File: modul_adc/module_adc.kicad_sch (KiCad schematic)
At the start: 26 parts

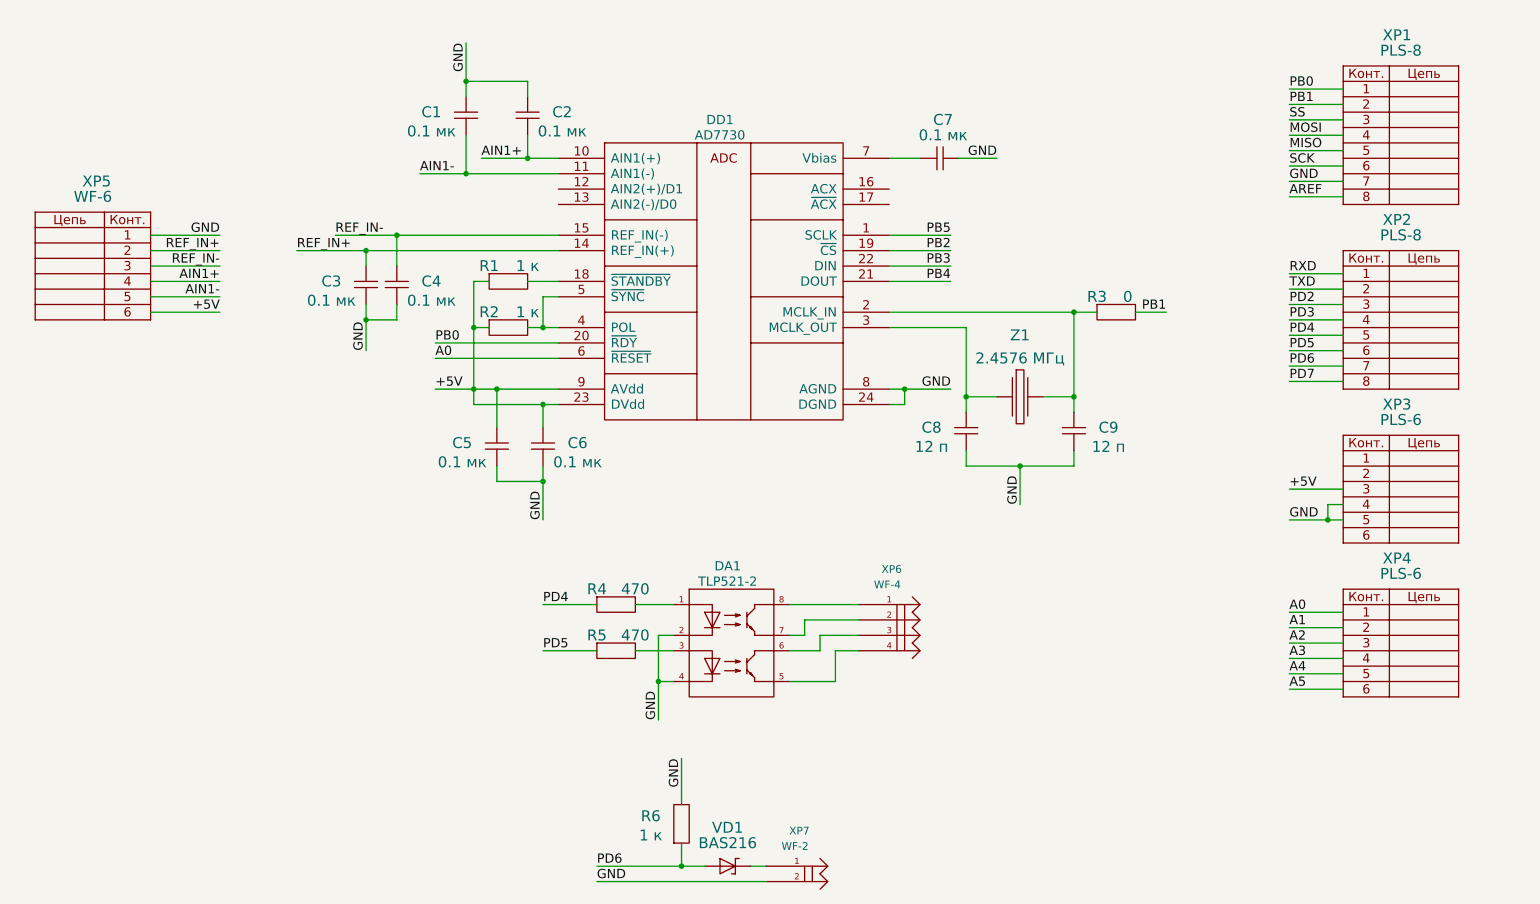
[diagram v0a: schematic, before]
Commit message: Дополнил схему ацп для тензодатчика и приступил к трассировке печатной платы.
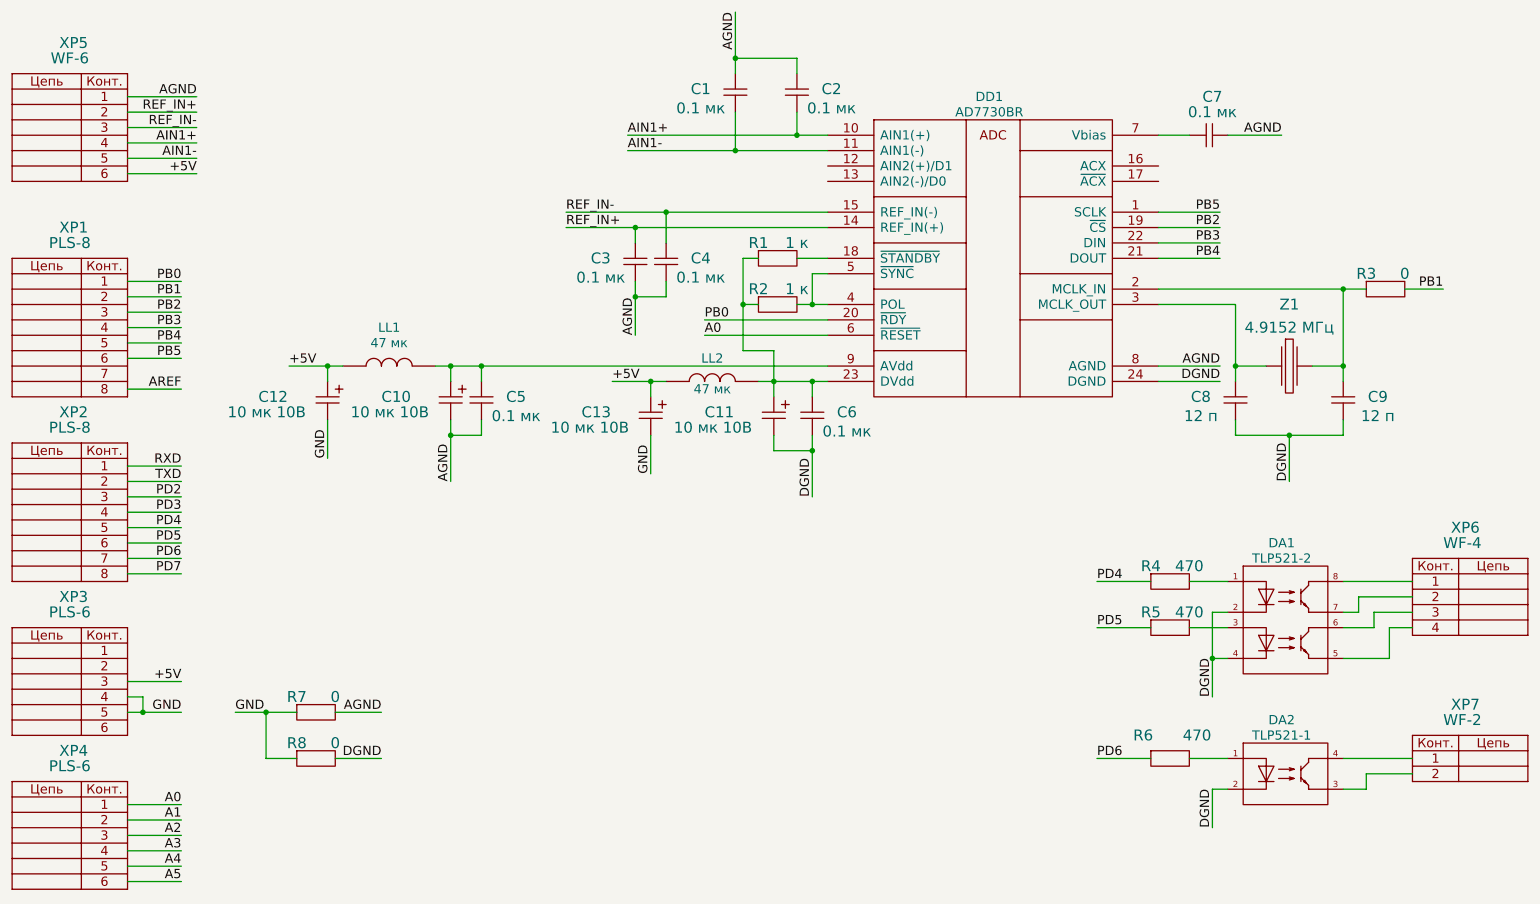
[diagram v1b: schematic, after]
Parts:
- removed VD1: BAS216, IWcomponents:SOD110, symbol module_adc-rescue:SHOTTKY_DIODE
- removed XP6: WF-4, IWconnectors:WF-4, symbol module_adc-rescue:PIN_M_4
- removed XP7: WF-2, IWconnectors:WF-2, symbol module_adc-rescue:PIN_M_2
- added C10, C11, C12, C13: 10 мк 10В, IWsmd_case:CASE_B, symbol LFcapitors:CAPITORS_ELECTROLYTIC
- added DA2: TLP521-1, IWcomponents:DIP_4, symbol LFcomponents:TLP521-1
- added LL1, LL2: 47 мк, IWsmd_case:SMD0805, symbol LFtransformator:INDUCTOR_3
- added R7, R8: 0, IWsmd_case:SMD0805, symbol module_adc-rescue:RESISTOR
- added XP6: WF-4, IWconnectors:WF-4, symbol LFconnectors:connector_4pin_gost
- added XP7: WF-2, IWconnectors:WF-2, symbol LFconnectors:connector_2pin_gost
- DD1: value AD7730 -> AD7730BR
- R6: value 1 к -> 470
- Z1: value 2.4576 МГц -> 4.9152 МГц; footprint IWcomponents:Q_49U3HMS& -> IWcomponents:HC-49SM
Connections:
- net MISO is gone; now on net PB4: XP1.5
- net MOSI is gone; now on net PB3: XP1.4
- net SCK is gone; now on net PB5: XP1.6
- net SS is gone; now on net PB2: XP1.3
- net +5V: now also C12.1, C13.1, LL1.2, LL2.2; no longer C5.1, C6.1, DD1.23 (DVdd), DD1.9 (AVdd), R1.1, R2.1
- net GND: now also C12.2, C13.2, R7.1, R8.1; no longer C1.1, C2.1, C3.2, C4.2, C5.2, C6.2, C7.1, C8.2, C9.2, DA1.2, DA1.4, DD1.24 (DGND), DD1.8 (AGND), R6.2, XP1.7, XP5.1
- net at DA1.5: now also XP6.4
- net at DA1.6: now also XP6.3
- net at DA1.7: now also XP6.2
- net at DA1.8: now also XP6.1
- new net: C11.1, C6.1, DD1.23 (DVdd), LL2.1, R1.1, R2.1
- new net: C10.1, C5.1, DD1.9 (AVdd), LL1.1
- new net: DA2.1, R6.2
- new net: DA2.4, XP7.1
- new net: DA2.3, XP7.2
- new net AGND: C1.1, C10.2, C2.1, C3.2, C4.2, C5.2, C7.1, DD1.8 (AGND), R7.2, XP5.1
- new net DGND: C11.2, C6.2, C8.2, C9.2, DA1.2, DA1.4, DA2.2, DD1.24 (DGND), R8.2
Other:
- moved on the sheet: C1, C2, C3, C4, C5, C6, C7, C8, C9, DA1, DD1, R1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

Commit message: Добавил обозначение разъёмов на схеме, поправил посадочное место кварца и отправил плату в производство.
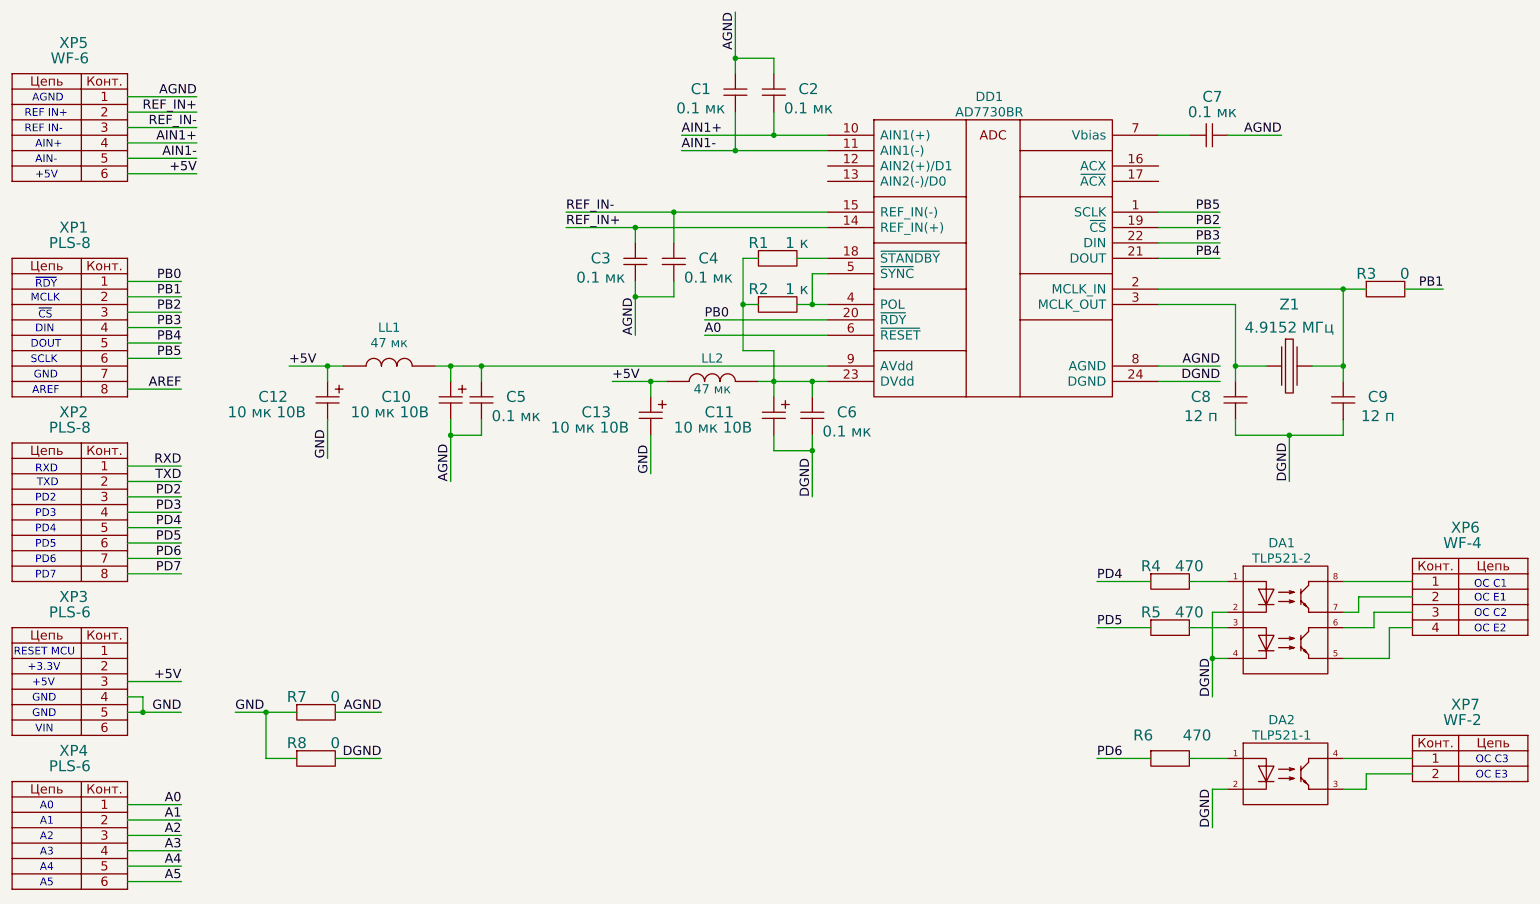
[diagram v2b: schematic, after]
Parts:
- Z1: footprint IWcomponents:HC-49SM -> IWcrystal_oscil:HC-49U
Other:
- note added: "+3.3V"
- note added: "+5V"
- note added: "A0"
- note added: "A1"
- note added: "A2"
- note added: "A3"
- note added: "A4"
- note added: "A5"
- note added: "AGND"
- note added: "AIN+"
- note added: "AIN-"
- note added: "AREF"
- note added: "DIN"
- note added: "DOUT"
- note added: "GND"
- note added: "MCLK"
- note added: "OC C1"
- note added: "OC C2"
- note added: "OC C3"
- note added: "OC E1"
- note added: "OC E2"
- note added: "OC E3"
- note added: "PD2"
- note added: "PD3"
- note added: "PD4"
- note added: "PD5"
- note added: "PD6"
- note added: "PD7"
- note added: "REF IN+"
- note added: "REF IN-"
- note added: "RESET MCU"
- note added: "RXD"
- note added: "SCLK"
- note added: "TXD"
- note added: "VIN"
- note added: "~{CS}"
- note added: "~{RDY}"
- moved on the sheet: C2, C4
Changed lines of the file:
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@@
   (junction (at 140.97 72.39) (diameter 0) (color 0 0 0 0)
   )
-  (junction (at 128.27 57.15) (diameter 0) (color 0 0 0 0)
+  (junction (at 129.54 57.15) (diameter 0) (color 0 0 0 0)
   )
   (junction (at 231.14 93.98) (diameter 0) (color 0 0 0 0)
   )
-  (junction (at 149.86 44.45) (diameter 0) (color 0 0 0 0)
+  (junction (at 146.05 44.45) (diameter 0) (color 0 0 0 0)
   )
   (junction (at 92.71 82.55) (diameter 0) (color 0 0 0 0)
@@
     (stroke (width 0) (type default))
   )
-  (wire (pts (xy 121.92 44.45) (xy 149.86 44.45))
+  (wire (pts (xy 130.81 44.45) (xy 146.05 44.45))
     (stroke (width 0) (type default))
   )
@@
     (stroke (width 0) (type default))
   )
-  (wire (pts (xy 128.27 57.15) (xy 154.94 57.15))
+  (wire (pts (xy 129.54 57.15) (xy 154.94 57.15))
     (stroke (width 0) (type default))
   )
@@
     (stroke (width 0) (type default))
   )
-  (wire (pts (xy 121.92 46.99) (xy 139.7 46.99))
+  (wire (pts (xy 130.81 46.99) (xy 139.7 46.99))
     (stroke (width 0) (type default))
   )
@@
     (stroke (width 0) (type default))
   )
-  (wire (pts (xy 149.86 40.64) (xy 149.86 44.45))
+  (wire (pts (xy 146.05 40.64) (xy 146.05 44.45))
     (stroke (width 0) (type default))
   )
@@
     (stroke (width 0) (type default))
   )
-  (wire (pts (xy 128.27 68.58) (xy 128.27 71.12))
+  (wire (pts (xy 129.54 68.58) (xy 129.54 71.12))
     (stroke (width 0) (type default))
   )
@@
     (stroke (width 0) (type default))
   )
-  (wire (pts (xy 128.27 71.12) (xy 123.19 71.12))
+  (wire (pts (xy 129.54 71.12) (xy 123.19 71.12))
     (stroke (width 0) (type default))
   )
@@
     (stroke (width 0) (type default))
   )
-  (wire (pts (xy 111.76 57.15) (xy 128.27 57.15))
+  (wire (pts (xy 111.76 57.15) (xy 129.54 57.15))
     (stroke (width 0) (type default))
   )
@@
     (stroke (width 0) (type default))
   )
-  (wire (pts (xy 128.27 62.23) (xy 128.27 57.15))
+  (wire (pts (xy 129.54 62.23) (xy 129.54 57.15))
     (stroke (width 0) (type default))
   )
@@
     (stroke (width 0) (type default))
   )
-  (wire (pts (xy 139.7 31.75) (xy 149.86 31.75))
+  (wire (pts (xy 139.7 31.75) (xy 146.05 31.75))
     (stroke (width 0) (type default))
   )
@@
     (stroke (width 0) (type default))
   )
-  (wire (pts (xy 149.86 31.75) (xy 149.86 34.29))
+  (wire (pts (xy 146.05 31.75) (xy 146.05 34.29))
     (stroke (width 0) (type default))
   )
@@
     (stroke (width 0) (type default))
   )
-  (wire (pts (xy 149.86 44.45) (xy 154.94 44.45))
+  (wire (pts (xy 146.05 44.45) (xy 154.94 44.45))
     (stroke (width 0) (type default))
   )
@@
     (stroke (width 0) (type default))
   )
+  (text "RESET MCU" (at 20.574 130.556 0)
+    (effects (font (size 1.27 1.27)) (justify left bottom))
+  )
+  (text "A2" (at 24.892 161.036 0)
+    (effects (font (size 1.27 1.27)) (justify left bottom))
+  )
+  (text "PD7" (at 24.13 117.856 0)
+    (effects (font (size 1.27 1.27)) (justify left bottom))
+  )
+  (text "PD4" (at 24.13 110.236 0)
+    (effects (font (size 1.27 1.27)) (justify left bottom))
+  )
+  (text "+5V" (at 24.13 51.816 0)
+    (effects (font (size 1.27 1.27)) (justify left bottom))
+  )
+  (text "OC E2" (at 261.62 126.746 0)
+    (effects (font (size 1.27 1.27)) (justify left bottom))
+  )
+  (text "MCLK" (at 23.368 72.136 0)
+    (effects (font (size 1.27 1.27)) (justify left bottom))
+  )
+  (text "OC C3" (at 261.874 148.336 0)
+    (effects (font (size 1.27 1.27)) (justify left bottom))
+  )
+  (text "RXD" (at 24.13 100.33 0)
+    (effects (font (size 1.27 1.27)) (justify left bottom))
+  )
+  (text "A5" (at 24.892 168.656 0)
+    (effects (font (size 1.27 1.27)) (justify left bottom))
+  )
+  (text "REF IN-" (at 22.352 44.196 0)
+    (effects (font (size 1.27 1.27)) (justify left bottom))
+  )
+  (text "TXD" (at 24.384 102.616 0)
+    (effects (font (size 1.27 1.27)) (justify left bottom))
+  )
+  (text "PD6" (at 24.13 115.316 0)
+    (effects (font (size 1.27 1.27)) (justify left bottom))
+  )
+  (text "PD2" (at 24.13 105.156 0)
+    (effects (font (size 1.27 1.27)) (justify left bottom))
+  )
+  (text "OC E1" (at 261.62 121.666 0)
+    (effects (font (size 1.27 1.27)) (justify left bottom))
+  )
+  (text "AGND" (at 23.622 39.116 0)
+    (effects (font (size 1.27 1.27)) (justify left bottom))
+  )
+  (text "VIN" (at 24.13 143.256 0)
+    (effects (font (size 1.27 1.27)) (justify left bottom))
+  )
+  (text "GND" (at 23.622 138.176 0)
+    (effects (font (size 1.27 1.27)) (justify left bottom))
+  )
+  (text "A3" (at 24.892 163.576 0)
+    (effects (font (size 1.27 1.27)) (justify left bottom))
+  )
+  (text "+5V" (at 23.622 135.636 0)
+    (effects (font (size 1.27 1.27)) (justify left bottom))
+  )
+  (text "OC C1" (at 261.62 119.38 0)
+    (effects (font (size 1.27 1.27)) (justify left bottom))
+  )
+  (text "AREF" (at 23.622 87.376 0)
+    (effects (font (size 1.27 1.27)) (justify left bottom))
+  )
+  (text "A1" (at 24.892 158.496 0)
+    (effects (font (size 1.27 1.27)) (justify left bottom))
+  )
+  (text "~{CS}" (at 24.638 74.93 0)
+    (effects (font (size 1.27 1.27)) (justify left bottom))
+  )
+  (text "OC E3" (at 261.874 150.876 0)
+    (effects (font (size 1.27 1.27)) (justify left bottom))
+  )
+  (text "A0" (at 24.892 155.956 0)
+    (effects (font (size 1.27 1.27)) (justify left bottom))
+  )
+  (text "GND" (at 23.622 140.716 0)
+    (effects (font (size 1.27 1.27)) (justify left bottom))
+  )
+  (text "GND" (at 23.876 84.836 0)
+    (effects (font (size 1.27 1.27)) (justify left bottom))
+  )
+  (text "AIN-" (at 24.13 49.276 0)
+    (effects (font (size 1.27 1.27)) (justify left bottom))
+  )
+  (text "OC C2" (at 261.62 124.206 0)
+    (effects (font (size 1.27 1.27)) (justify left bottom))
+  )
+  (text "A4" (at 24.892 166.116 0)
+    (effects (font (size 1.27 1.27)) (justify left bottom))
+  )
+  (text "DOUT" (at 23.368 79.756 0)
+    (effects (font (size 1.27 1.27)) (justify left bottom))
+  )
+  (text "AIN+" (at 24.13 46.736 0)
+    (effects (font (size 1.27 1.27)) (justify left bottom))
+  )
+  (text "DIN" (at 24.13 77.216 0)
+    (effects (font (size 1.27 1.27)) (justify left bottom))
+  )
+  (text "PD3" (at 24.13 107.696 0)
+    (effects (font (size 1.27 1.27)) (justify left bottom))
+  )
+  (text "~{RDY}" (at 24.13 69.85 0)
+    (effects (font (size 1.27 1.27)) (justify left bottom))
+  )
+  (text "PD5" (at 24.13 112.776 0)
+    (effects (font (size 1.27 1.27)) (justify left bottom))
+  )
+  (text "+3.3V" (at 22.86 133.096 0)
+    (effects (font (size 1.27 1.27)) (justify left bottom))
+  )
+  (text "REF IN+" (at 22.352 41.656 0)
+    (effects (font (size 1.27 1.27)) (justify left bottom))
+  )
+  (text "SCLK" (at 23.368 82.296 0)
+    (effects (font (size 1.27 1.27)) (justify left bottom))
+  )
   (label "REF_IN-" (at 111.76 57.15 0) (fields_autoplaced)
     (effects (font (size 1.524 1.524)) (justify left bottom))
@@
     (effects (font (size 1.524 1.524)) (justify right bottom))
   )
-  (label "AIN1-" (at 121.92 46.99 0) (fields_autoplaced)
+  (label "AIN1-" (at 130.81 46.99 0) (fields_autoplaced)
     (effects (font (size 1.524 1.524)) (justify left bottom))
   )
@@
     (effects (font (size 1.524 1.524)) (justify left bottom))
   )
-  (label "AIN1+" (at 121.92 44.45 0) (fields_autoplaced)
+  (label "AIN1+" (at 130.81 44.45 0) (fields_autoplaced)
     (effects (font (size 1.524 1.524)) (justify left bottom))
   )
@@
     )
   )
-  (symbol (lib_id "module_adc-rescue:CAPITORS") (at 149.86 34.29 270) (unit 1)
-    (in_bom yes) (on_board yes) (dnp no)
-    (property "Reference" "C2" (at 155.575 36.83 90)
-      (effects (font (size 1.8034 1.8034)))
-    )
-    (property "Value" "0.1 мк" (at 155.575 40.005 90)
-      (effects (font (size 1.8034 1.8034)))
-    )
-    (property "Footprint" "IWsmd_case:SMD0805" (at 149.86 34.29 0)
-      (effects (font (size 1.524 1.524)) hide)
-    )
-    (property "Datasheet" "" (at 149.86 34.29 0)
+  (symbol (lib_id "module_adc-rescue:CAPITORS") (at 146.05 34.29 270) (unit 1)
+    (in_bom yes) (on_board yes) (dnp no)
+    (property "Reference" "C2" (at 151.765 36.83 90)
+      (effects (font (size 1.8034 1.8034)))
+    )
+    (property "Value" "0.1 мк" (at 151.765 40.005 90)
+      (effects (font (size 1.8034 1.8034)))
+    )
+    (property "Footprint" "IWsmd_case:SMD0805" (at 146.05 34.29 0)
+      (effects (font (size 1.524 1.524)) hide)
+    )
+    (property "Datasheet" "" (at 146.05 34.29 0)
       (effects (font (size 1.524 1.524)) hide)
     )
@@
     )
   )
-  (symbol (lib_id "module_adc-rescue:CAPITORS") (at 128.27 62.23 270) (unit 1)
-    (in_bom yes) (on_board yes) (dnp no)
-    (property "Reference" "C4" (at 133.985 64.77 90)
-      (effects (font (size 1.8034 1.8034)))
-    )
-    (property "Value" "0.1 мк" (at 133.985 67.945 90)
-      (effects (font (size 1.8034 1.8034)))
-    )
-    (property "Footprint" "IWsmd_case:SMD0805" (at 128.27 62.23 0)
-      (effects (font (size 1.524 1.524)) hide)
-    )
-    (property "Datasheet" "" (at 128.27 62.23 0)
+  (symbol (lib_id "module_adc-rescue:CAPITORS") (at 129.54 62.23 270) (unit 1)
+    (in_bom yes) (on_board yes) (dnp no)
+    (property "Reference" "C4" (at 135.255 64.77 90)
+      (effects (font (size 1.8034 1.8034)))
+    )
+    (property "Value" "0.1 мк" (at 135.255 67.945 90)
+      (effects (font (size 1.8034 1.8034)))
+    )
+    (property "Footprint" "IWsmd_case:SMD0805" (at 129.54 62.23 0)
+      (effects (font (size 1.524 1.524)) hide)
+    )
+    (property "Datasheet" "" (at 129.54 62.23 0)
       (effects (font (size 1.524 1.524)) hide)
     )
@@
       (effects (font (size 1.8034 1.8034)))
     )
-    (property "Footprint" "IWcomponents:HC-49SM" (at 227.33 82.55 0)
-      (effects (font (size 1.524 1.524)) hide)
-    )
+    (property "Footprint" "IWcrystal_oscil:HC-49U" (at 227.33 82.55 0)
+      (effects (font (size 1.524 1.524)) hide)
+    )
